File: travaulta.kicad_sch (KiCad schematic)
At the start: 30 parts

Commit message: schematics
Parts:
- gave numbers to parts that had none: 30

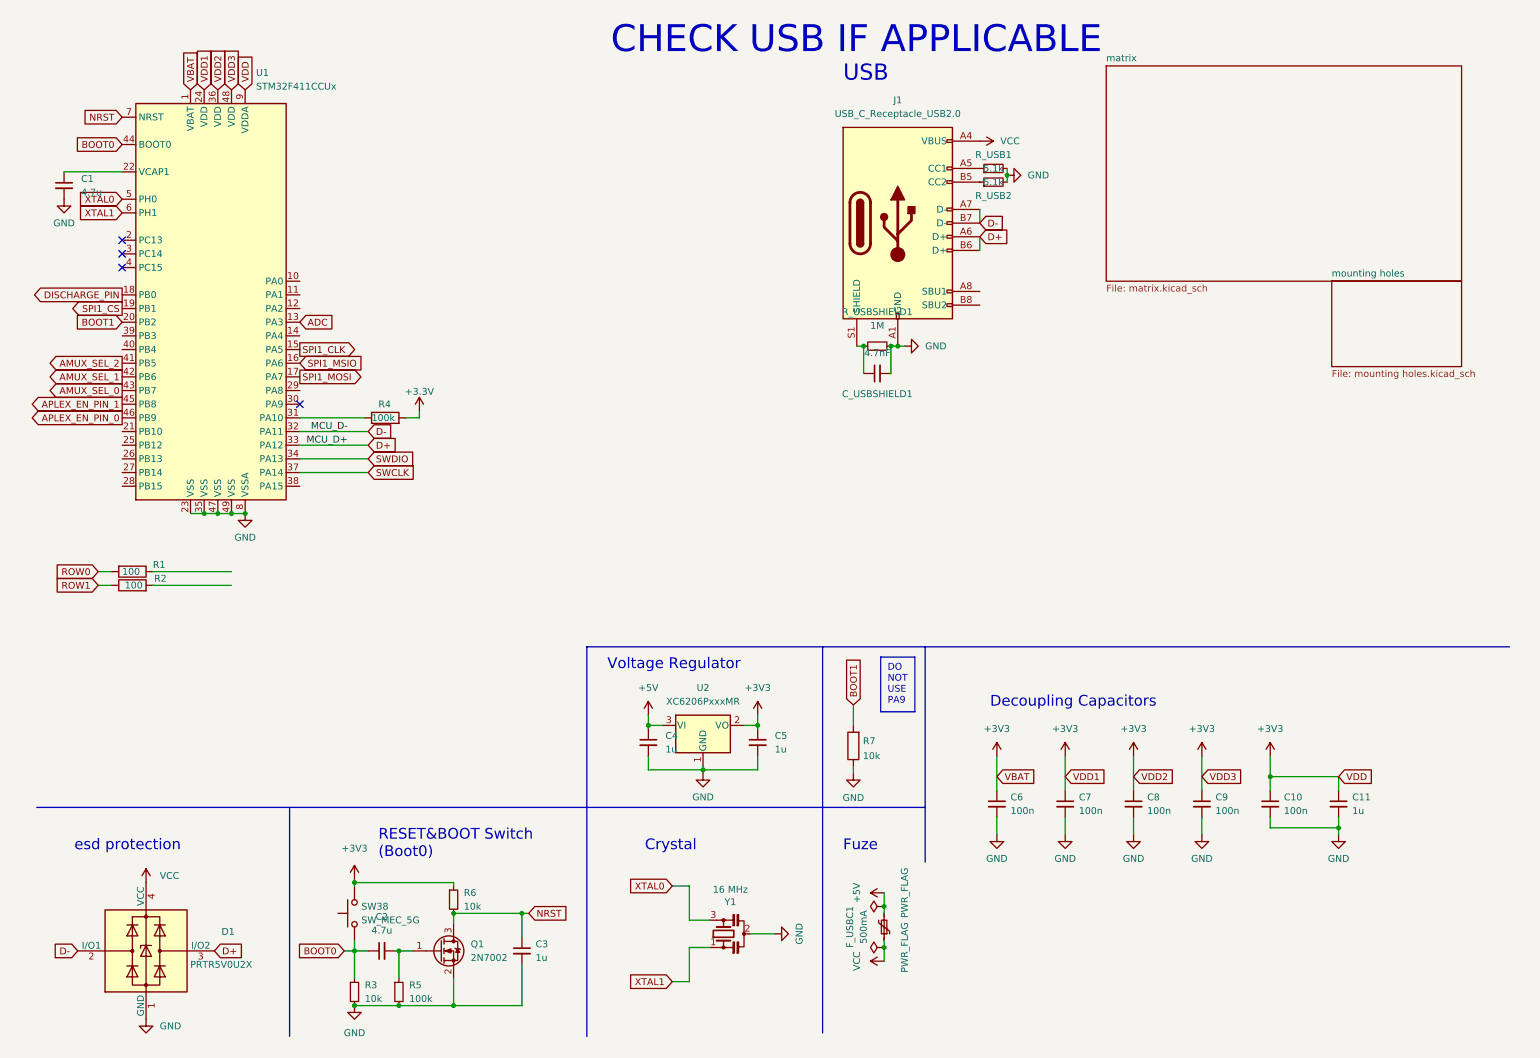
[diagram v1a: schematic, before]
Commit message: analog schematics added
some questions
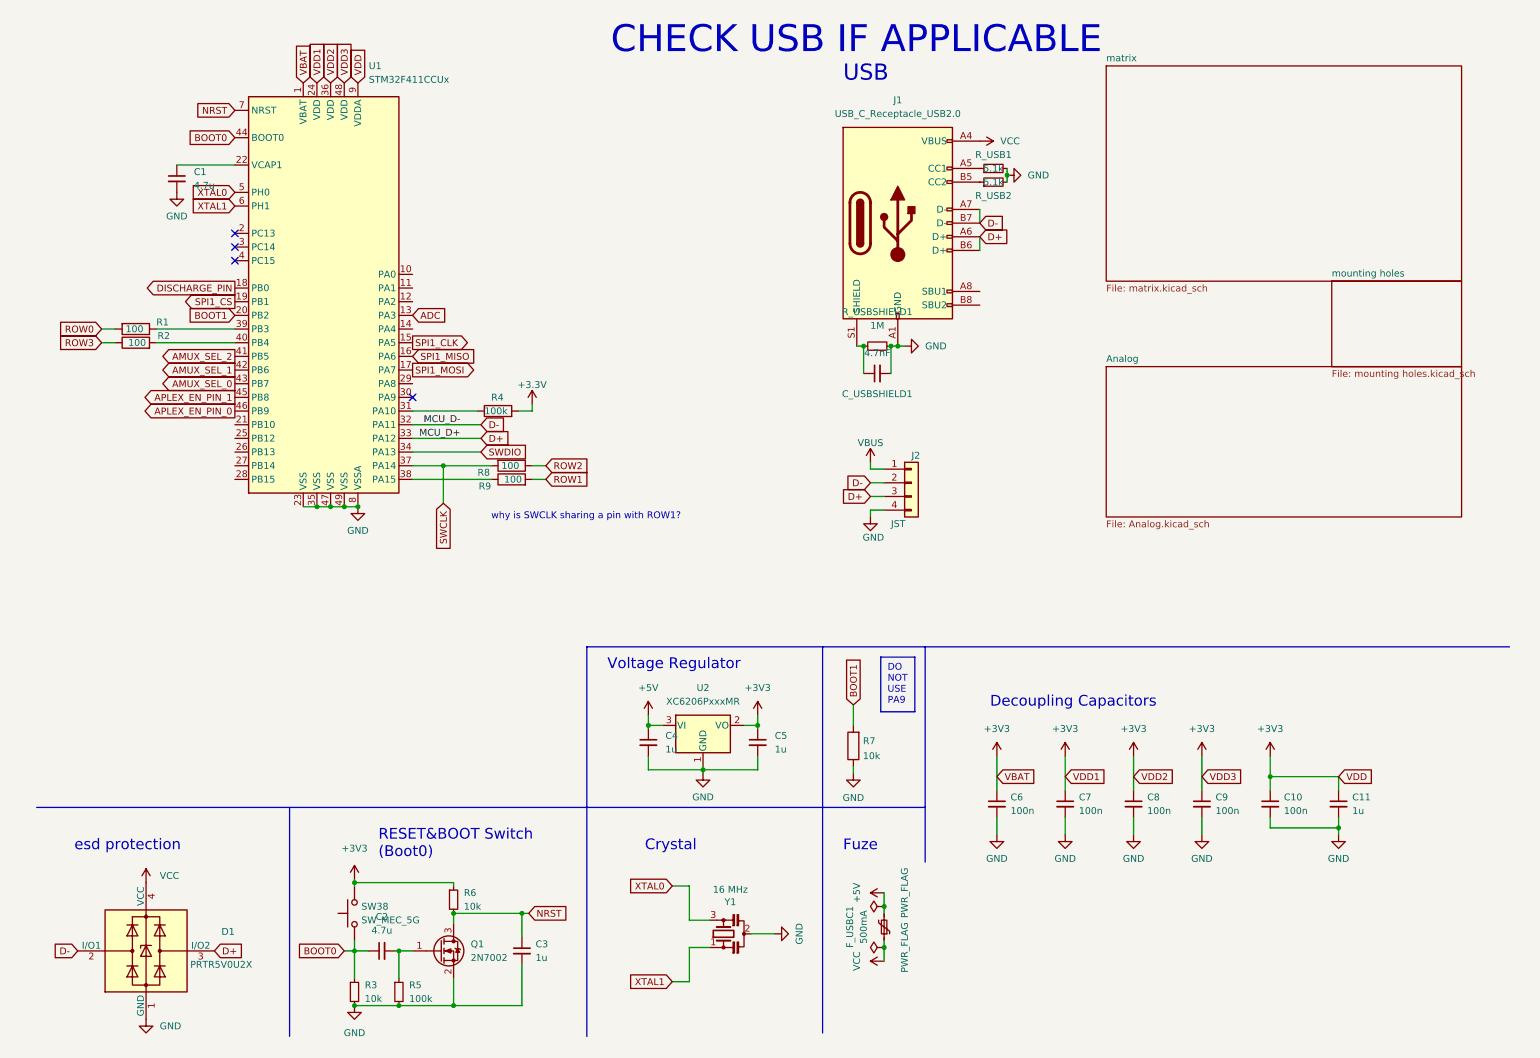
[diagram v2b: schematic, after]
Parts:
- added J2: JST, cipulot_parts:JST-SR-4, symbol Connector_Generic:Conn_01x04
- added R8, R9: 100, Resistor_SMD:R_0402_1005Metric, symbol Device:R
- C1, C10, C11, C2, C3, C4, C5, C6, C7, C8, C9: footprint (none) -> Capacitor_SMD:C_0402_1005Metric
- R3, R5, R6: footprint (none) -> Resistor_SMD:R_0402_1005Metric
- SW38: footprint (none) -> cipulot_parts:SW_SPST_TL3342
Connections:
- net D+: now also J2.3 (Pin_3)
- net D-: now also J2.2 (Pin_2)
- net GND: now also J2.4 (Pin_4)
- net ROW1: now also R9.2; no longer R2.1
- net SWCLK: now also R8.2
- net at R1.1: now also U1.39 (PB3)
- net at R2.2: now also U1.40 (PB4)
- net at U1.38 (PA15): now also R9.1
- net SPI1_MSIO renamed SPI1_MISO
- new net ROW2: R8.1
- new net ROW3: R2.1
- new net VBUS: J2.1 (Pin_1)
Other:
- added sheet Analog (Analog.kicad_sch)
- note added: "why is SWCLK sharing a pin with ROW1?"
- moved on the sheet: C1, R1, R2, R4, U1

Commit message: autosave
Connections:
- net VBUS is gone; now on net VCC: J2.1 (Pin_1)
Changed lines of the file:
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@@
     (pin "2")
+  )
+  (symbol (lib_id "power:VCC") (at 167.005 91.44 0) (unit 1)
+    (in_bom yes) (on_board yes) (fields_autoplaced)
+    (property "Reference" "#PWR?" (id 0) (at 167.005 95.25 0)
+      (effects (font (size 1.27 1.27)) hide)
+    )
+    (property "Value" "VCC" (id 1) (at 168.91 90.1699 0)
+      (effects (font (size 1.27 1.27)) (justify left))
+    )
+    (property "Footprint" "" (id 2) (at 167.005 91.44 0)
+      (effects (font (size 1.27 1.27)) hide)
+    )
+    (property "Datasheet" "" (id 3) (at 167.005 91.44 0)
+      (effects (font (size 1.27 1.27)) hide)
+    )
+    (pin "1")
   )
   (symbol (lib_id "power:+5V") (at 169.545 171.45 90) (unit 1)
@@
     )
     (property "Datasheet" "" (id 3) (at 190.5 146.05 0)
-      (effects (font (size 1.27 1.27)) hide)
-    )
-    (pin "1")
-  )
-  (symbol (lib_id "power:VBUS") (at 167.005 91.44 0) (unit 1)
-    (in_bom yes) (on_board yes) (fields_autoplaced)
-    (property "Reference" "#PWR0132" (id 0) (at 167.005 95.25 0)
-      (effects (font (size 1.27 1.27)) hide)
-    )
-    (property "Value" "VBUS" (id 1) (at 167.005 87.8355 0))
-    (property "Footprint" "" (id 2) (at 167.005 91.44 0)
-      (effects (font (size 1.27 1.27)) hide)
-    )
-    (property "Datasheet" "" (id 3) (at 167.005 91.44 0)
       (effects (font (size 1.27 1.27)) hide)
     )
@@
       (reference "#PWR0131") (unit 1) (value "GND") (footprint "")
     )
-    (path "/d12ca525-ee4e-4ed0-aa99-b4c82c0e9279"
-      (reference "#PWR0132") (unit 1) (value "VBUS") (footprint "")
-    )
     (path "/4fc14b43-29bb-4139-9959-9ded495ce088"
       (reference "#PWR0133") (unit 1) (value "GND") (footprint "")
@@
       (reference "#PWR0148") (unit 1) (value "GND") (footprint "")
     )
+    (path "/9a5b8bd9-4139-474e-9b39-f68af6bab2a6"
+      (reference "#PWR?") (unit 1) (value "VCC") (footprint "")
+    )
     (path "/3e19c7b5-727f-4d33-8900-0016dbf9cc71"

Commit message: early routing
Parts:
- removed C_USBSHIELD1: 4.7nF, Capacitor_SMD:C_0402_1005Metric, symbol Device:C_Small
- removed J1: USB_C_Receptacle_USB2.0, Connector_USB:USB_C_Receptacle_HRO_TYPE-C-31-M-12, symbol Connector:USB_C_Receptacle_USB2.0
- removed R_USB1, R_USB2: 5.1k, Resistor_SMD:R_0402_1005Metric, symbol Device:R_Small
- removed R_USBSHIELD1: 1M, Resistor_SMD:R_0402_1005Metric, symbol Device:R_Small
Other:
- note added: "JST"
- note removed: "CHECK USB IF APPLICABLE"
- note removed: "USB"
- moved on the sheet: J2

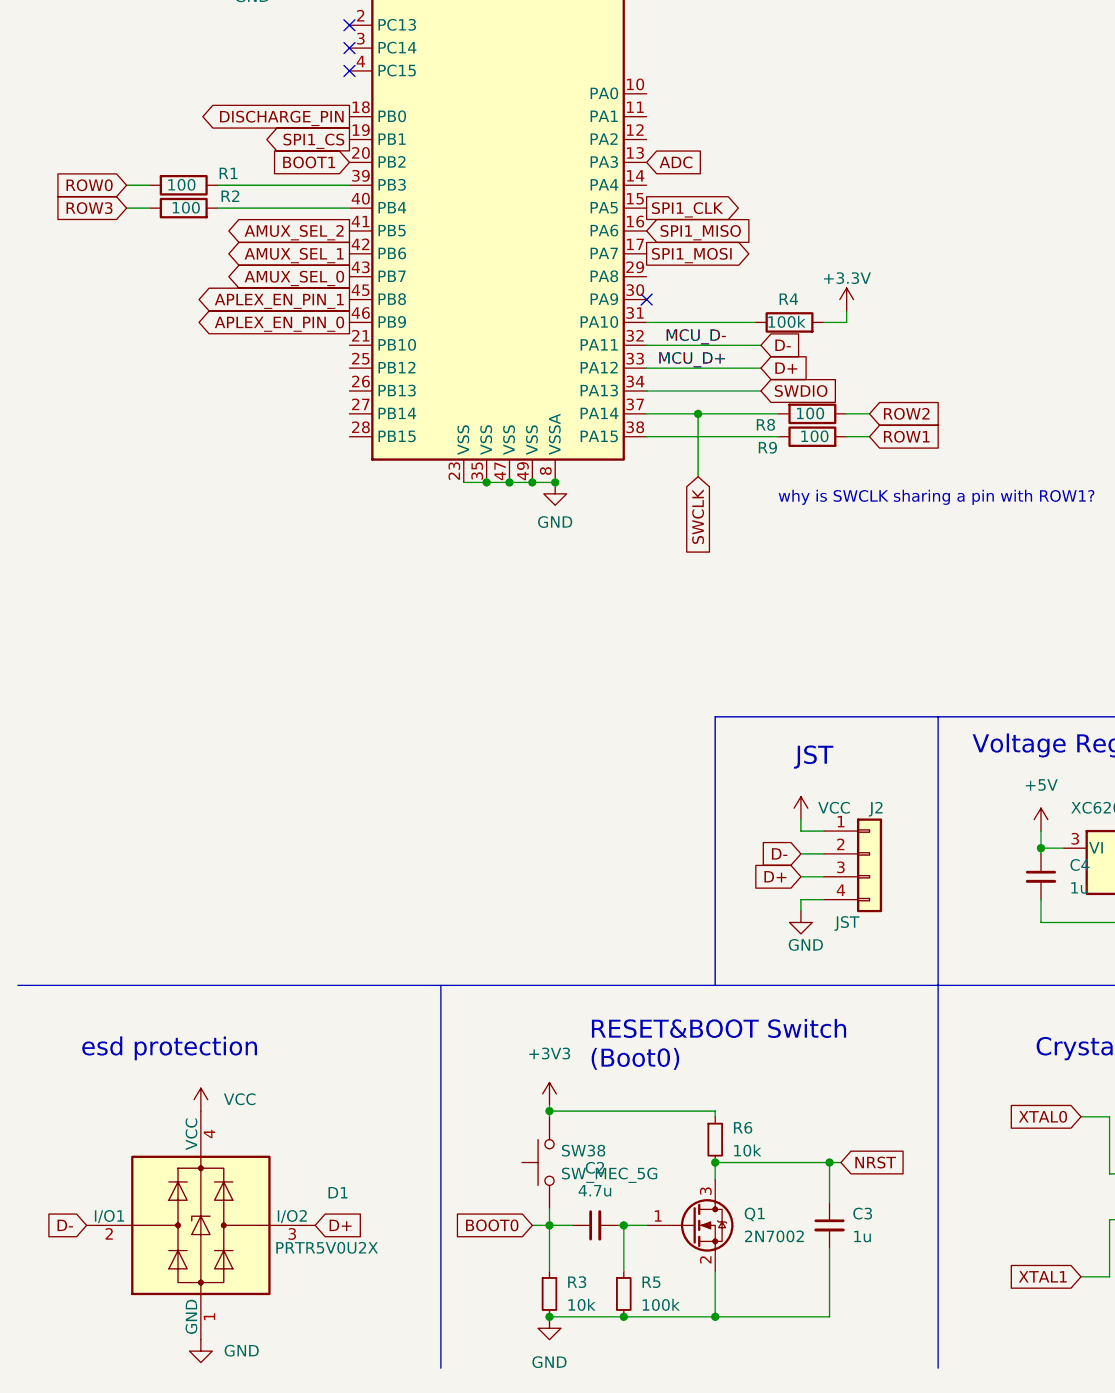
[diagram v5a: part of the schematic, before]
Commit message: component placement
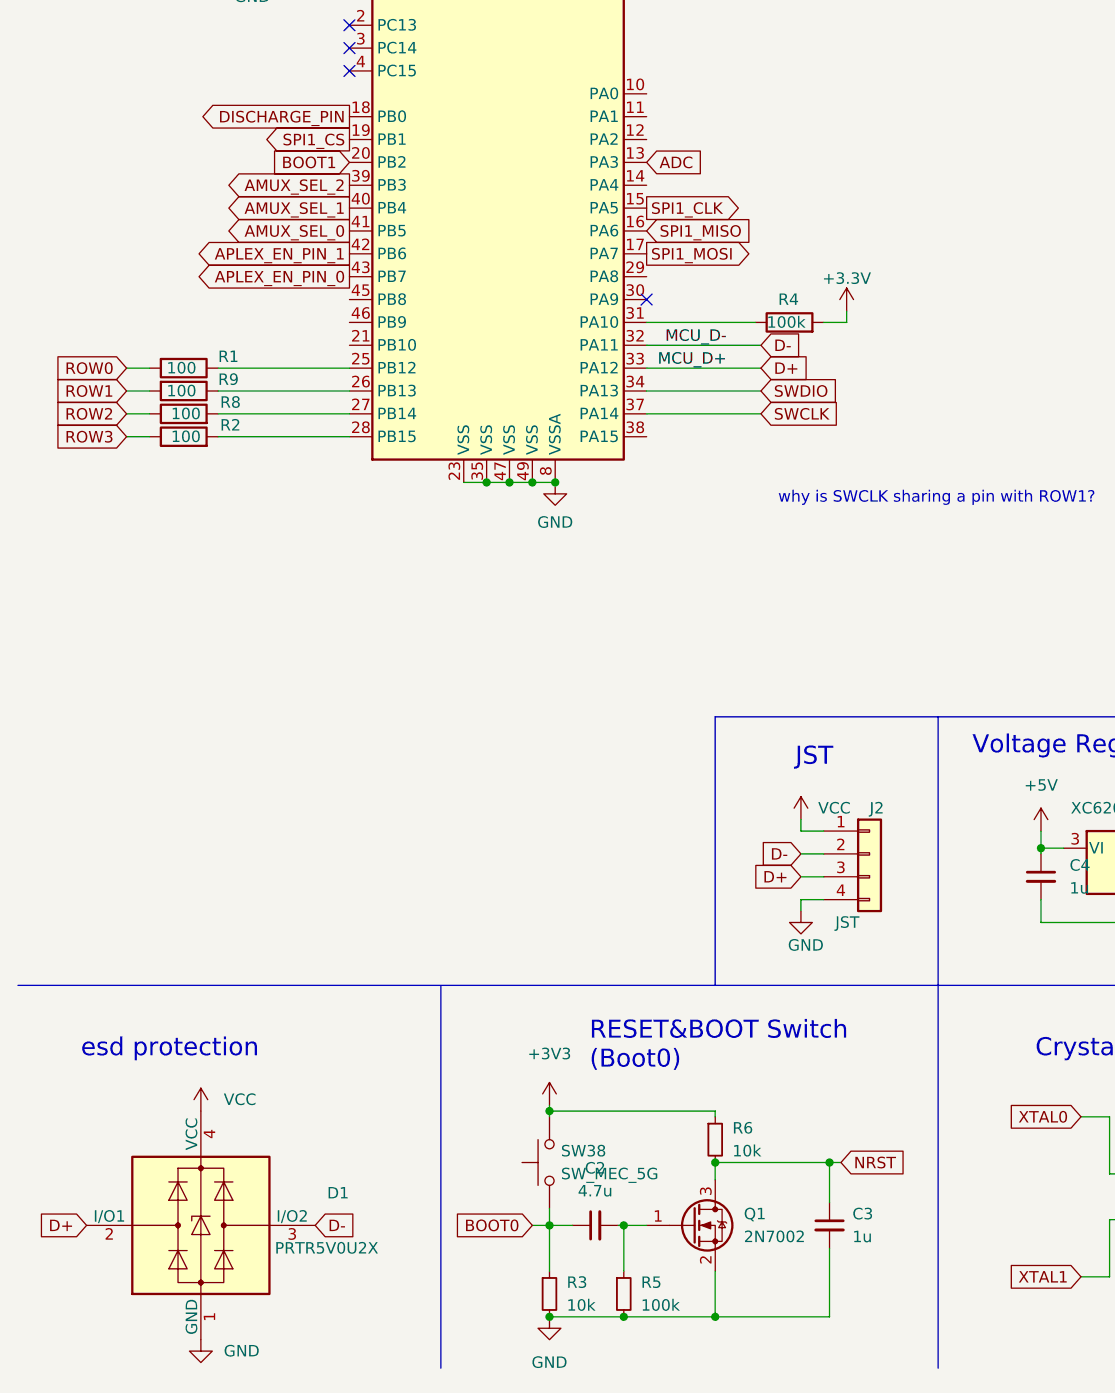
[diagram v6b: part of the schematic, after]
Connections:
- net AMUX_SEL_0: now also U1.41 (PB5); no longer U1.43 (PB7)
- net AMUX_SEL_1: now also U1.40 (PB4); no longer U1.42 (PB6)
- net AMUX_SEL_2: now also U1.39 (PB3); no longer U1.41 (PB5)
- net APLEX_EN_PIN_0: now also U1.43 (PB7); no longer U1.46 (PB9)
- net APLEX_EN_PIN_1: now also U1.42 (PB6); no longer U1.45 (PB8)
- net D+: now also D1.2 (I/O1); no longer D1.3 (I/O2)
- net D-: now also D1.3 (I/O2); no longer D1.2 (I/O1)
- net SWCLK: no longer R8.2
- net at R1.1: now also U1.25 (PB12); no longer U1.39 (PB3)
- net at R2.2: now also U1.28 (PB15); no longer U1.40 (PB4)
- net at U1.26 (PB13): now also R9.1
- net at U1.27 (PB14): now also R8.2
- net at U1.38 (PA15): no longer R9.1
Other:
- moved on the sheet: R1, R2, R8, R9

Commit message: routing work
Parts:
- added R18, R24: 5.1k, Resistor_SMD:R_0402_1005Metric, symbol Device:R
- added USB1: TYPEC-304YSSW-ACP16, cipulot_parts:TYPEC-304YSSW-ACP16, symbol cipulot_parts:TYPEC-304YSSW-ACP16
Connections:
- net D+: now also USB1.6 (DP1), USB1.8 (DP2)
- net D-: now also USB1.5 (DN2), USB1.7 (DN1)
- net GND: now also R18.1, R24.2, USB1.1 (GND), USB1.12 (GND), USB1.13 (SHIELD)
- net VCC: now also USB1.11 (VBUS), USB1.2 (VBUS)
- new net: R24.1, USB1.10 (CC2)
- new net: R18.2, USB1.4 (CC1)
- no-connect marks 4 -> 6
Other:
- note added: "USB-C"
- note added: "can i exchange vbus for vcc?"
- note removed: "why is SWCLK sharing a pin with ROW1?"
